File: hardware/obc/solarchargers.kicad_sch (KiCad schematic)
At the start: 36 parts, among them U105 LTC4121, U402 LTC4121

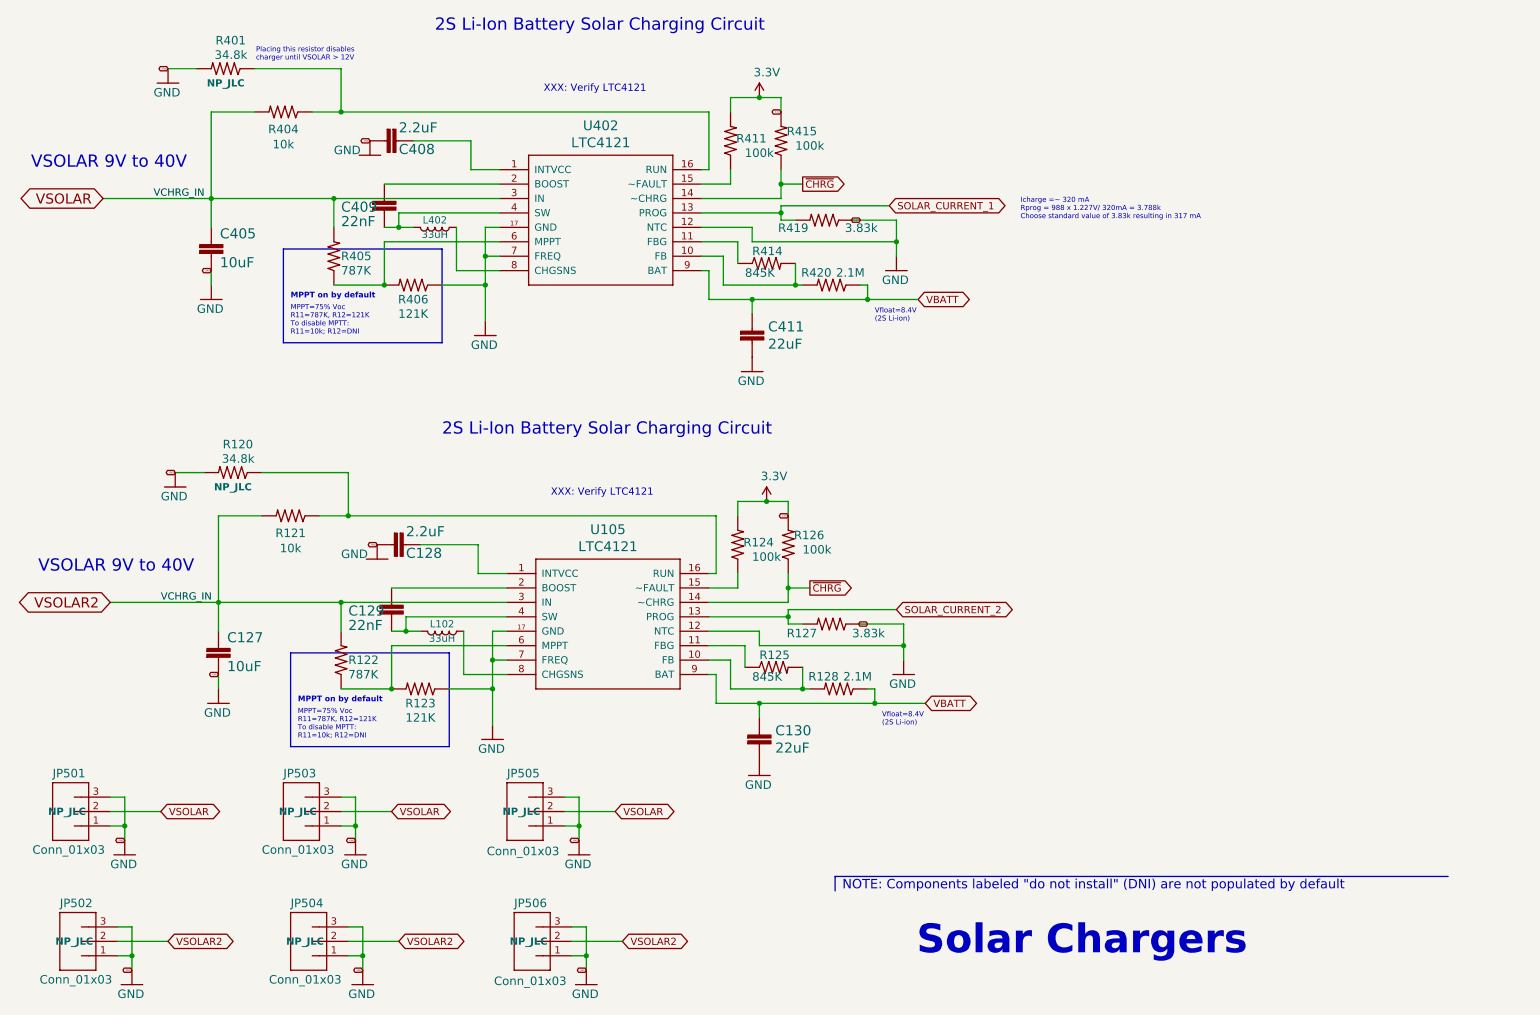
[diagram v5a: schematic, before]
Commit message: obc: refactors and renumbers
- renumber pages for more logical review order
- renumber reference designators to get smaller numbers
- small changes to layout from early design review
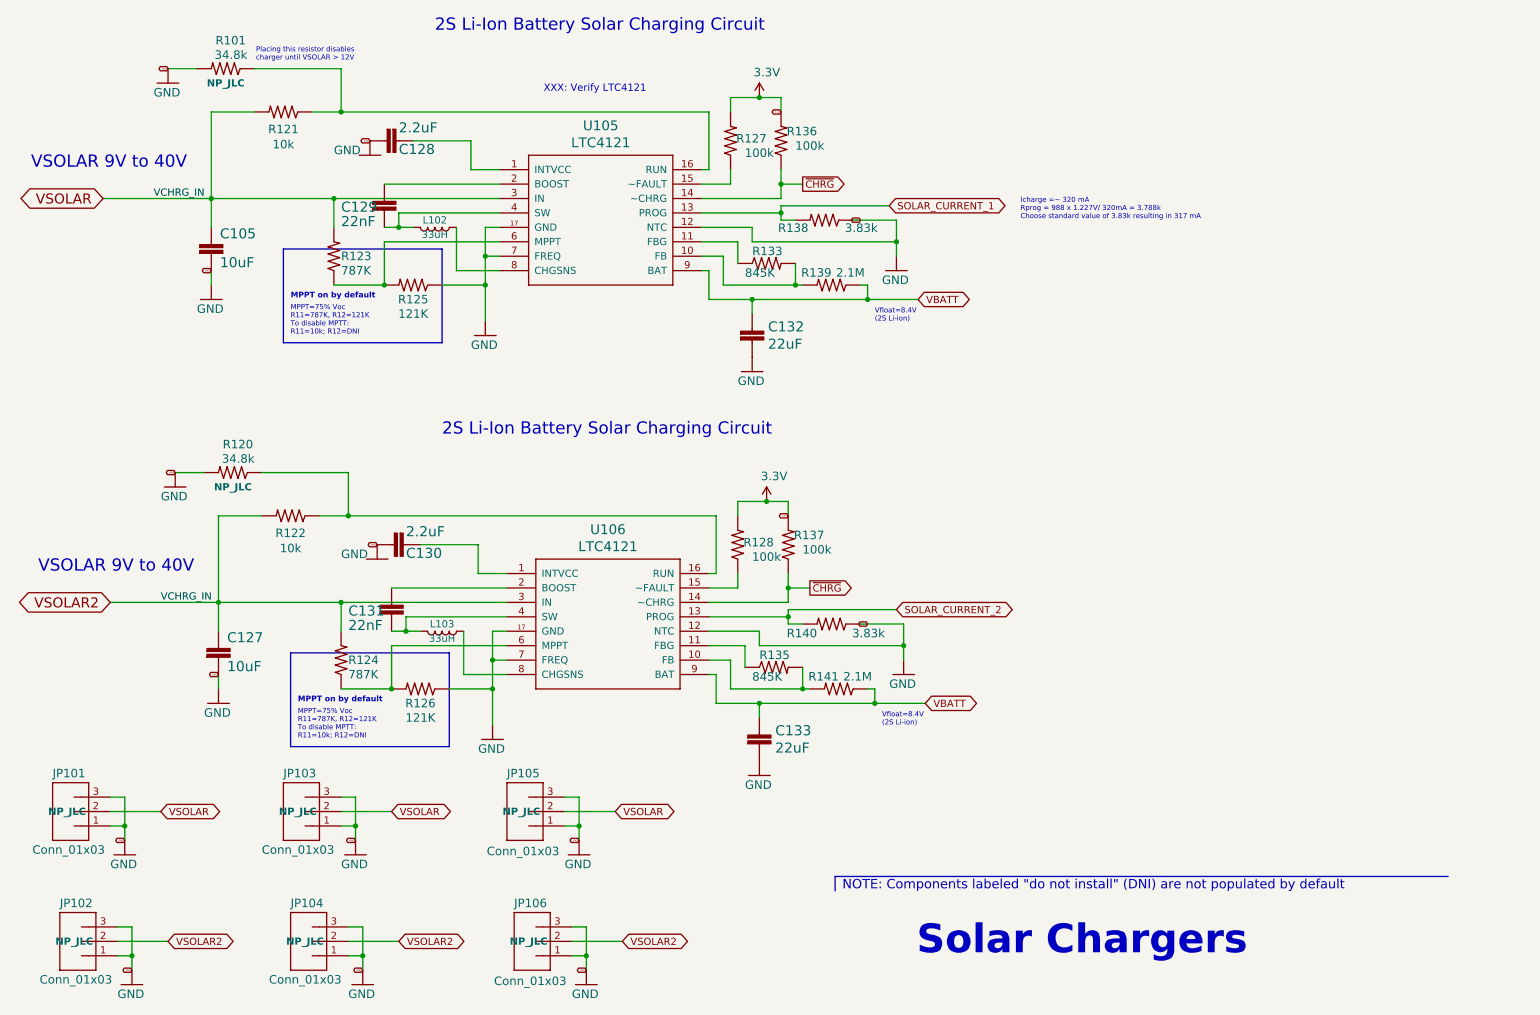
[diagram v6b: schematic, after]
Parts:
- renumbered C405 to C105, C408 to C128, C409 to C129, C128 to C130, C129 to C131, C411 to C132, C130 to C133, JP501 to JP101, JP502 to JP102, JP503 to JP103, JP504 to JP104, JP505 to JP105, JP506 to JP106, L402 to L102, L102 to L103, R401 to R101, R404 to R121, R121 to R122, R405 to R123, R122 to R124, R406 to R125, R123 to R126, R411 to R127, R124 to R128, R414 to R133, R125 to R135, R415 to R136, R126 to R137, R419 to R138, R420 to R139, R127 to R140, R128 to R141, U402 to U105, U105 to U106

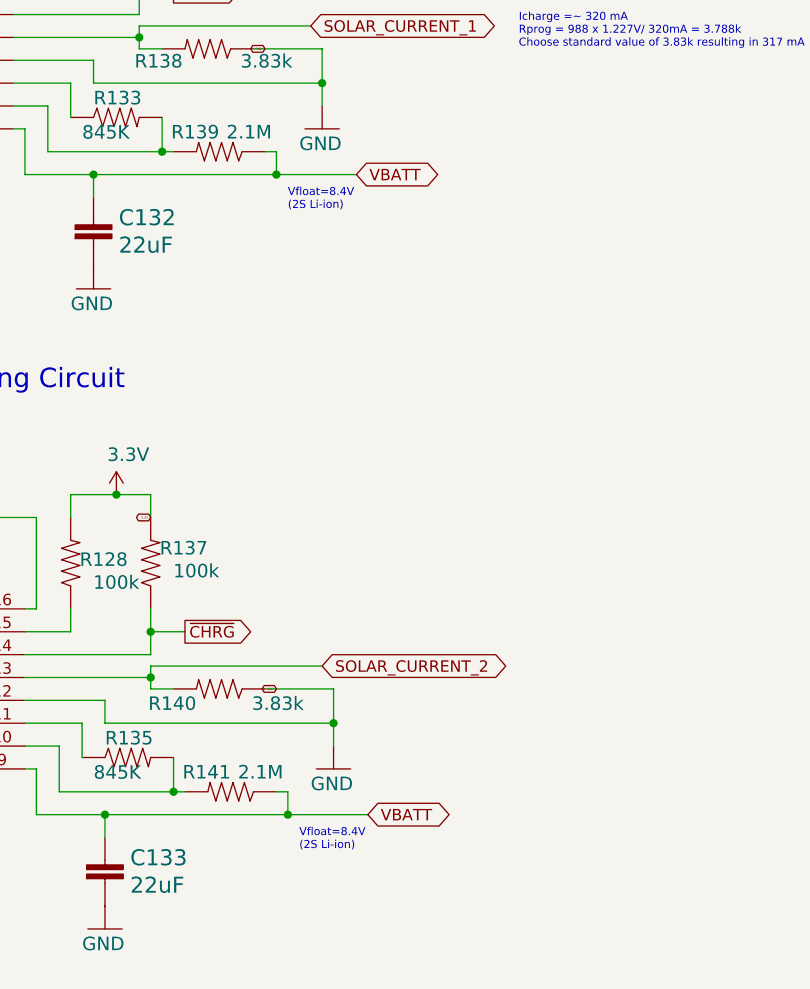
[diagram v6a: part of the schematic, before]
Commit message: obc: rename power nets for sanity
We've been confused by this for too long.

GNDREF -> PACKNEG
VCHRG -> PACKPOS
VBATT -> VRAIL
VBATT_SENSE -> INH_POS

Also add an OBC power subsystem diagram.
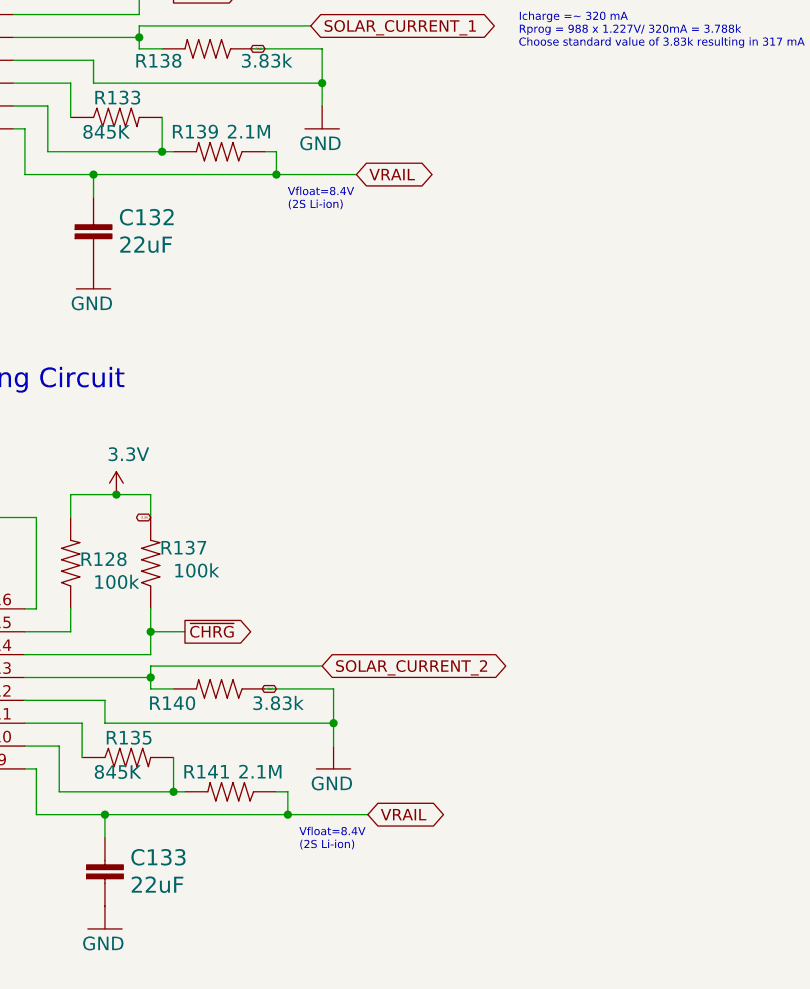
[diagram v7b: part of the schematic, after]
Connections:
- net VBATT renamed VRAIL
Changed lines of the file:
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@@
 		)
 	)
-	(global_label "VBATT"
+	(global_label "VRAIL"
 		(shape bidirectional)
 		(at 175.26 138.43 0)
@@
 		)
 	)
-	(global_label "VBATT"
+	(global_label "VRAIL"
 		(shape bidirectional)
 		(at 173.99 67.31 0)

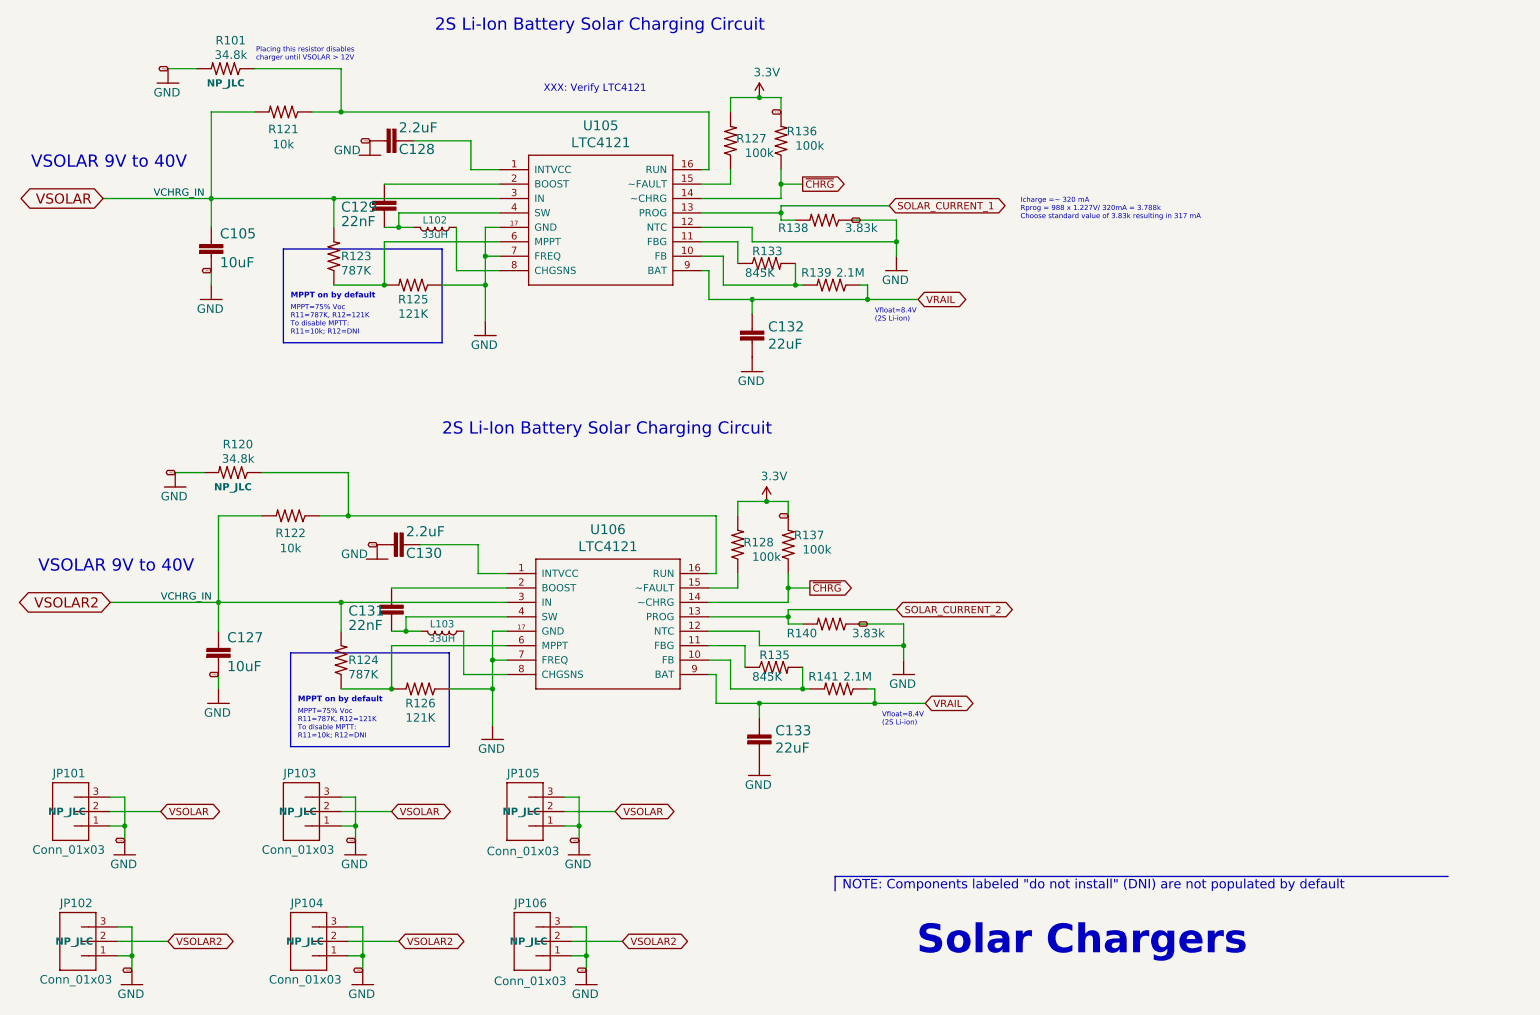
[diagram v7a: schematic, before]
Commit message: obc: Many schematic cleanups
Mostly alignment of components, adjustment of text.

Change SPI resistors to 27 ohms.
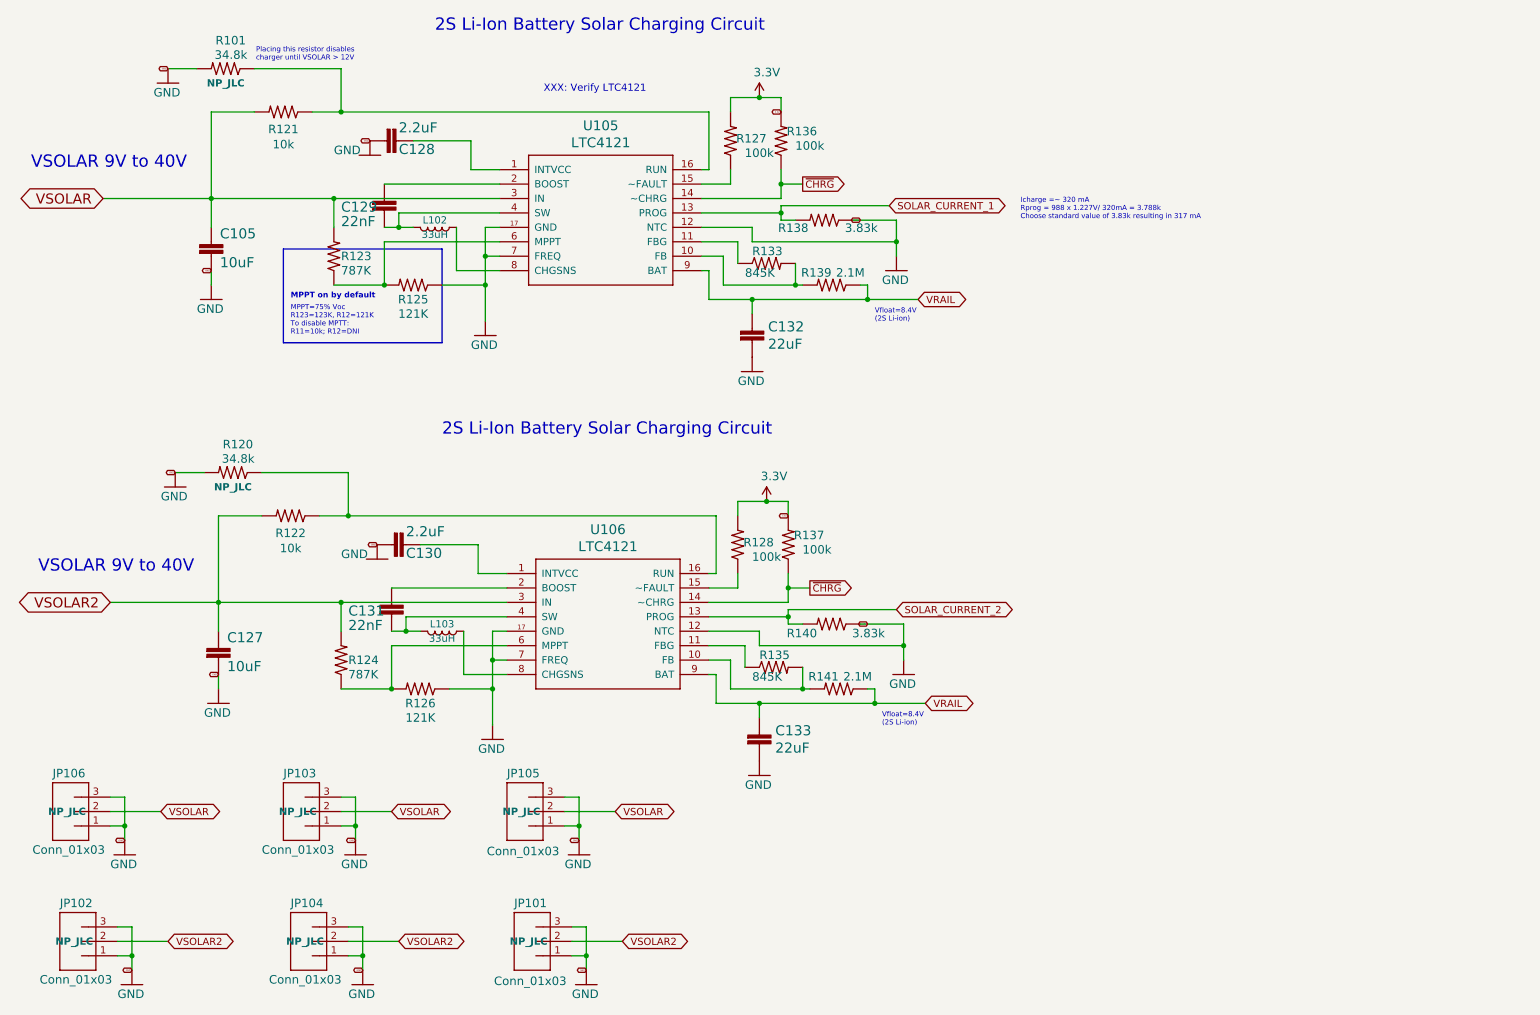
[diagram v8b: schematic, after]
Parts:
- renumbered JP106 to JP101, JP101 to JP106
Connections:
- net VSOLAR: no longer C127.1, JP101.2, JP102.2, JP104.2, R122.2, R124.2, U106.3 (IN)
- new net VSOLAR2: C127.1, JP101.2, JP102.2, JP104.2, R122.2, R124.2, U106.3 (IN)
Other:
- note added: "MPPT=75% Voc R123=123K, R12=121K To disable MPTT: R11=10k; R12=DNI"
- note removed: "MPPT=75% Voc R11=787K, R12=121K To disable MPTT: R11=10k; R12=DNI"
- note removed: "NOTE: Components labeled "do not install" (DNI) are not populated by default"
- note removed: "Solar Chargers"
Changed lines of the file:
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@@
 		(rev "1")
 		(company "Luke Titi, Michael Lyle")
+		(comment 2 "NOTE: Components labeled \"do not install\" (DNI) are not populated by default")
 	)
 	(junction
@@
 		)
 	)
-	(polyline
-		(pts
-			(xy 91.44 129.54) (xy 63.5 129.54)
-		)
-		(stroke
-			(width 0)
-			(type default)
-		)
-	)
 	(wire
 		(pts
@@
 		)
 	)
-	(polyline
-		(pts
-			(xy 91.44 146.05) (xy 91.44 129.54)
-		)
-		(stroke
-			(width 0)
-			(type default)
-		)
-	)
 	(wire
 		(pts
@@
 		)
 	)
-	(polyline
-		(pts
-			(xy 63.5 146.05) (xy 91.44 146.05)
-		)
-		(stroke
-			(width 0)
-			(type default)
-		)
-	)
 	(wire
 		(pts
@@
 		)
 	)
-	(polyline
-		(pts
-			(xy 159.385 171.45) (xy 159.385 168.91)
-		)
-		(stroke
-			(width 0)
-			(type default)
-		)
-	)
 	(wire
 		(pts
@@
 		)
 	)
-	(polyline
-		(pts
-			(xy 159.385 168.91) (xy 267.335 168.91)
-		)
-		(stroke
-			(width 0)
-			(type default)
-		)
-	)
 	(wire
 		(pts
@@
 		)
 	)
-	(polyline
-		(pts
-			(xy 63.5 129.54) (xy 63.5 146.05)
-		)
-		(stroke
-			(width 0)
-			(type default)
-		)
-	)
 	(wire
 		(pts
@@
 		)
 	)
-	(text "NOTE: Components labeled \"do not install\" (DNI) are not populated by default"
-		(exclude_from_sim no)
-		(at 160.655 171.45 0)
-		(effects
-			(font
-				(size 1.651 1.651)
-			)
-			(justify left bottom)
-		)
-	)
 	(text "XXX: Verify LTC4121"
 		(exclude_from_sim no)
@@
 		)
 	)
-	(text "\nMPPT=75% Voc\nR11=787K, R12=121K\nTo disable MPTT:\nR11=10k; R12=DNI"
+	(text "\nMPPT=75% Voc\nR123=123K, R12=121K\nTo disable MPTT:\nR11=10k; R12=DNI"
 		(exclude_from_sim no)
 		(at 63.5 73.66 0)
@@
 		)
 	)
-	(text "Solar Chargers"
-		(exclude_from_sim no)
-		(at 173.736 183.134 0)
-		(effects
-			(font
-				(size 5.08 5.08)
-				(thickness 1.016)
-				(bold yes)
-			)
-			(justify left bottom)
-		)
-	)
-	(text "\nMPPT=75% Voc\nR11=787K, R12=121K\nTo disable MPTT:\nR11=10k; R12=DNI"
-		(exclude_from_sim no)
-		(at 64.77 144.78 0)
-		(effects
-			(font
-				(size 0.889 0.889)
-			)
-			(justify left bottom)
-		)
-	)
 	(text "2S Li-Ion Battery Solar Charging Circuit"
 		(exclude_from_sim no)
@@
 		)
 	)
-	(text "MPPT on by default"
-		(exclude_from_sim no)
-		(at 64.77 138.43 0)
-		(effects
-			(font
-				(size 0.9906 0.9906)
-				(thickness 0.1981)
-				(bold yes)
-			)
-			(justify left bottom)
-		)
-	)
 	(text "Icharge =~ 320 mA\nRprog = 988 x 1.227V/ 320mA = 3.788k\nChoose standard value of 3.83k resulting in 317 mA"
 		(exclude_from_sim no)
@@
 		)
 	)
-	(label "VCHRG_IN"
-		(at 39.37 49.53 0)
-		(fields_autoplaced yes)
-		(effects
-			(font
-				(size 1.27 1.27)
-			)
-			(justify left bottom)
-		)
-	)
-	(label "VCHRG_IN"
-		(at 40.64 120.65 0)
-		(fields_autoplaced yes)
-		(effects
-			(font
-				(size 1.27 1.27)
-			)
-			(justify left bottom)
-		)
-	)
 	(global_label "VRAIL"
 		(shape bidirectional)
@@
 		(on_board yes)
 		(dnp no)
-		(property "Reference" "JP106"
+		(property "Reference" "JP101"
 			(at 102.87 174.498 0)
 			(effects
@@
 			(project "mainboard"
 				(path "/e3ac22ea-6806-4807-a025-571315789c25/5728bec1-e38c-4cf8-8d7a-17e9d882a72f"
-					(reference "JP106")
+					(reference "JP101")
 					(unit 1)
 				)
@@
 		(on_board yes)
 		(dnp no)
-		(property "Reference" "JP101"
+		(property "Reference" "JP106"
 			(at 21.59 151.638 0)
 			(effects
@@
 			(project "mainboard"
 				(path "/e3ac22ea-6806-4807-a025-571315789c25/5728bec1-e38c-4cf8-8d7a-17e9d882a72f"
-					(reference "JP101")
+					(reference "JP106")
 					(unit 1)
 				)
